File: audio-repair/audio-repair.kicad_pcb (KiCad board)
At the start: 2 copper layers, 64 x 17.8 mm, 27 parts, among them J1 Ext. Power, J2 Switchcraft_35RAPC4BHN3, J3 PL, J4 Speaker, J5 UVP, U1 PAM8019KGR, U2 1bitsy-basic-stubby

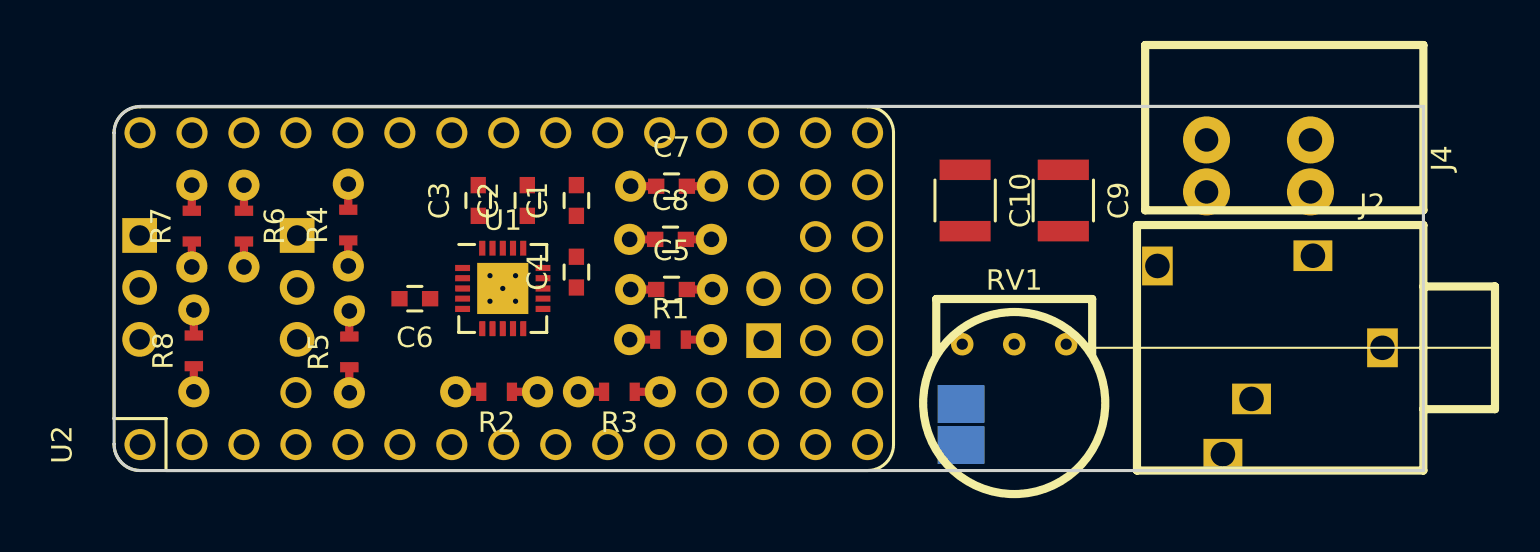
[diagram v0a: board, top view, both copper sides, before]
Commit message: Align through-hole components to 0.1" grid.
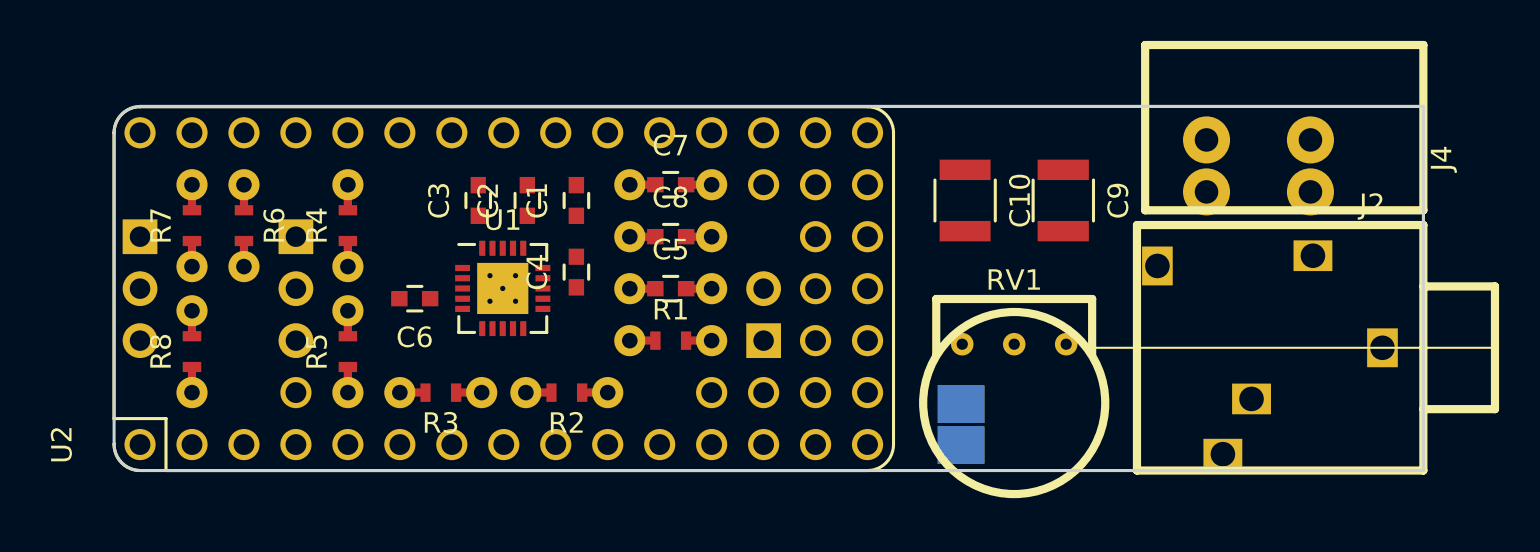
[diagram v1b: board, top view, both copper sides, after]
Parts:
- moved R3 10.7 mm to (114.0, 106.2)
- moved C7 2.04 mm to (125.2, 96.0)
- moved C5 2.04 mm to (125.2, 101.1)
- moved R7 2.02 mm to (103.8, 96.0)
- moved R5 2.01 mm to (111.4, 102.2)
- moved R1 2.01 mm to (129.2, 103.7)
- moved C8 1.99 mm to (125.2, 98.6)
- moved R6 1.98 mm to (106.3, 100.0)
- moved R4 1.97 mm to (111.4, 96.0)
- moved R8 1.96 mm to (103.8, 102.2)
- moved R2 1.43 mm to (120.1, 106.2)
- moved J3 0.08 mm to (108.9, 98.6)
- moved J5 0.06 mm to (101.3, 98.6)

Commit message: Route all traces except ground pours.
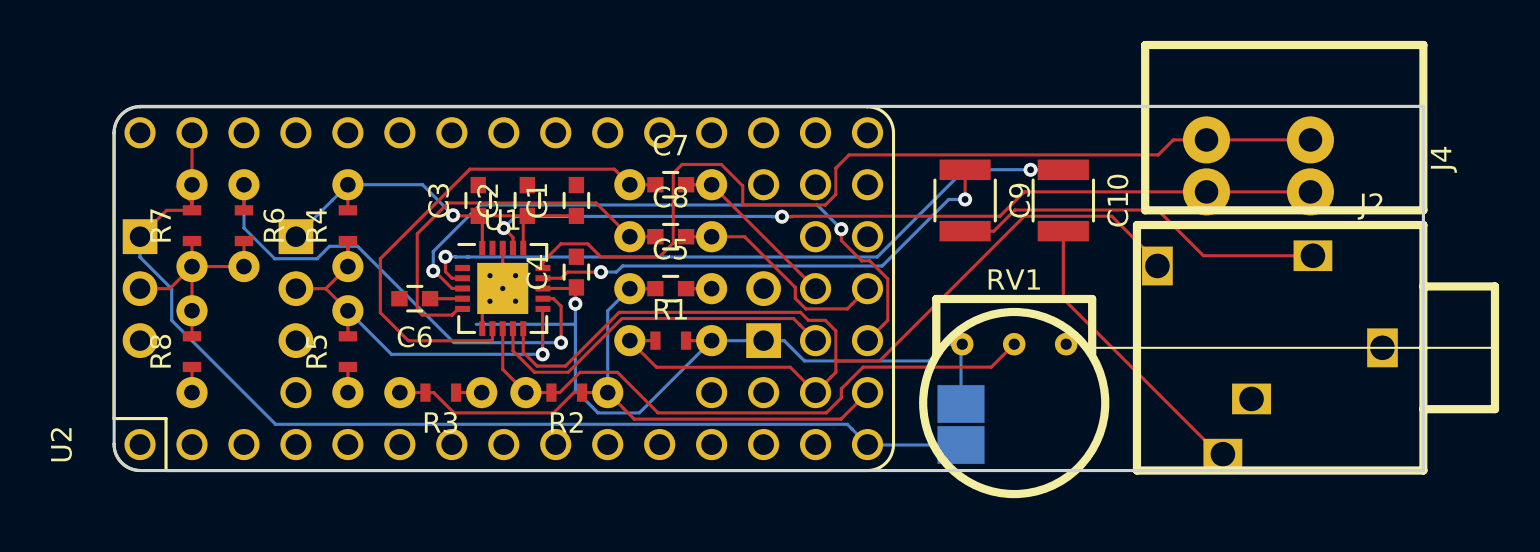
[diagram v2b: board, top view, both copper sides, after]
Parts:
- moved C10 4.80 mm to (146.4, 96.8)
- moved C9 4.80 mm to (141.6, 96.8)
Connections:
- U2 pad 1: (no net) -> GND
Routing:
- net VDD: track 0.00 -> 57.3 mm, vias 0 -> 2
- net +3V3: track 0.00 -> 54.1 mm
- net /TIP_SW: track 0.00 -> 52.8 mm
- net Net-(J4-Pad2): track 0.00 -> 45.8 mm
- net Net-(J4-Pad1): track 0.00 -> 41.4 mm, vias 0 -> 2
- net Net-(C10-Pad1): track 0.00 -> 33.8 mm, vias 0 -> 2
- net /VOL_ADC: track 0.00 -> 31.5 mm
- net /~SHUTDOWN: track 0.00 -> 31.1 mm, vias 0 -> 2
- net Net-(R2-Pad1): track 0.00 -> 30.3 mm
- net Net-(C7-Pad1): track 0.00 -> 24.8 mm
- net Net-(R6-Pad2): track 0.00 -> 24.5 mm, vias 0 -> 1
- net Net-(C9-Pad1): track 0.00 -> 23.7 mm, vias 0 -> 2
- net Net-(J3-Pad2): track 0.00 -> 20.6 mm, vias 0 -> 1
- net Net-(C8-Pad1): track 0.00 -> 19.1 mm
- net Net-(C9-Pad2): track 0.00 -> 18.4 mm
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
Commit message: Pour grounds, clean up silkscreen.
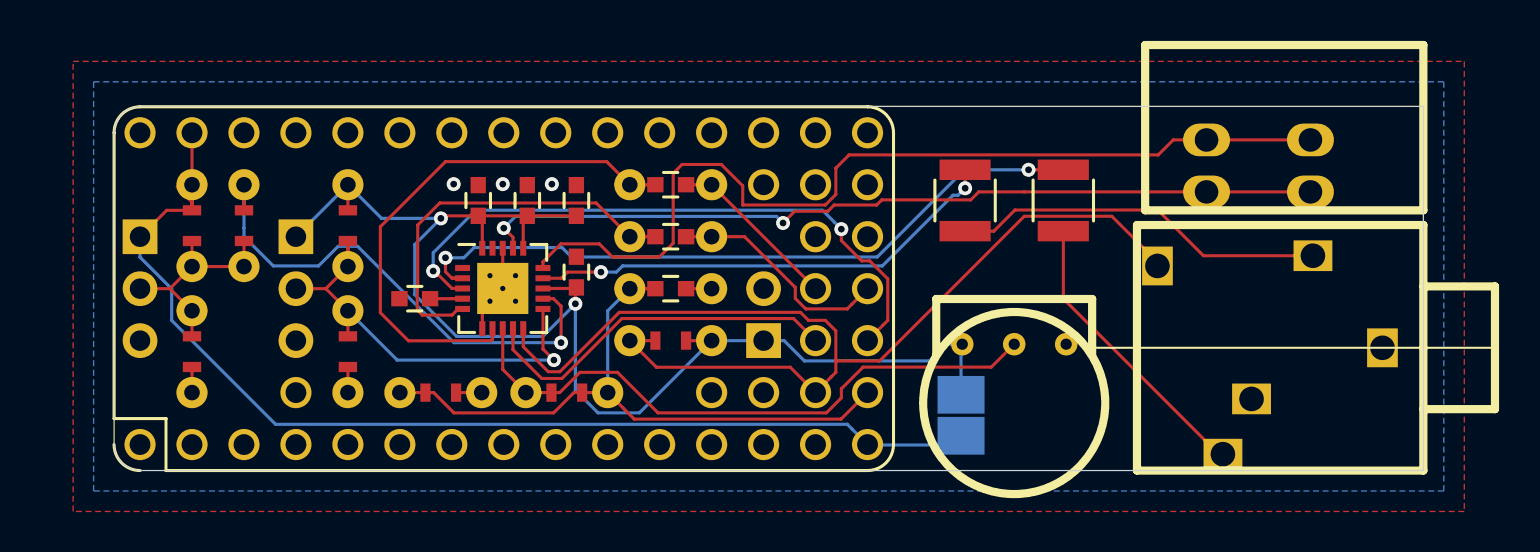
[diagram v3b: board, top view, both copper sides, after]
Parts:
- 3v3 Pwr: renamed from JP1
- PL Adj: renamed from J3
- UVP Adj: renamed from J5
- moved 3v3 Pwr 0.45 mm to (141.4, 107.3)
- renumbered J1 to Pwr
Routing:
- net VDD: track 57.3 -> 66.2 mm
- net Net-(C7-Pad1): track 24.8 -> 26.0 mm
- net Net-(J3-Pad2): track 20.6 -> 21.7 mm
- net GND: track 13.1 -> 14.0 mm
- net Net-(C10-Pad1): track 33.8 -> 34.5 mm
- net Net-(J5-Pad2): track 11.4 -> 10.8 mm
- net Net-(R6-Pad2): track 24.5 -> 25.0 mm
- net (no net): vias 0 -> 3
- added copper zone on B.Cu, net GND
- added copper zone on F.Cu, net GND
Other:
- board text added: "1Bitsy DAC Audio"
